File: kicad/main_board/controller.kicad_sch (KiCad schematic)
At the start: 44 parts, among them J6 FRONT_PANEL, J7 I2C, J8 SWD, U7 MCP4728, U8 RP2040, U9 W25Q128JVP, Y1 12MHz

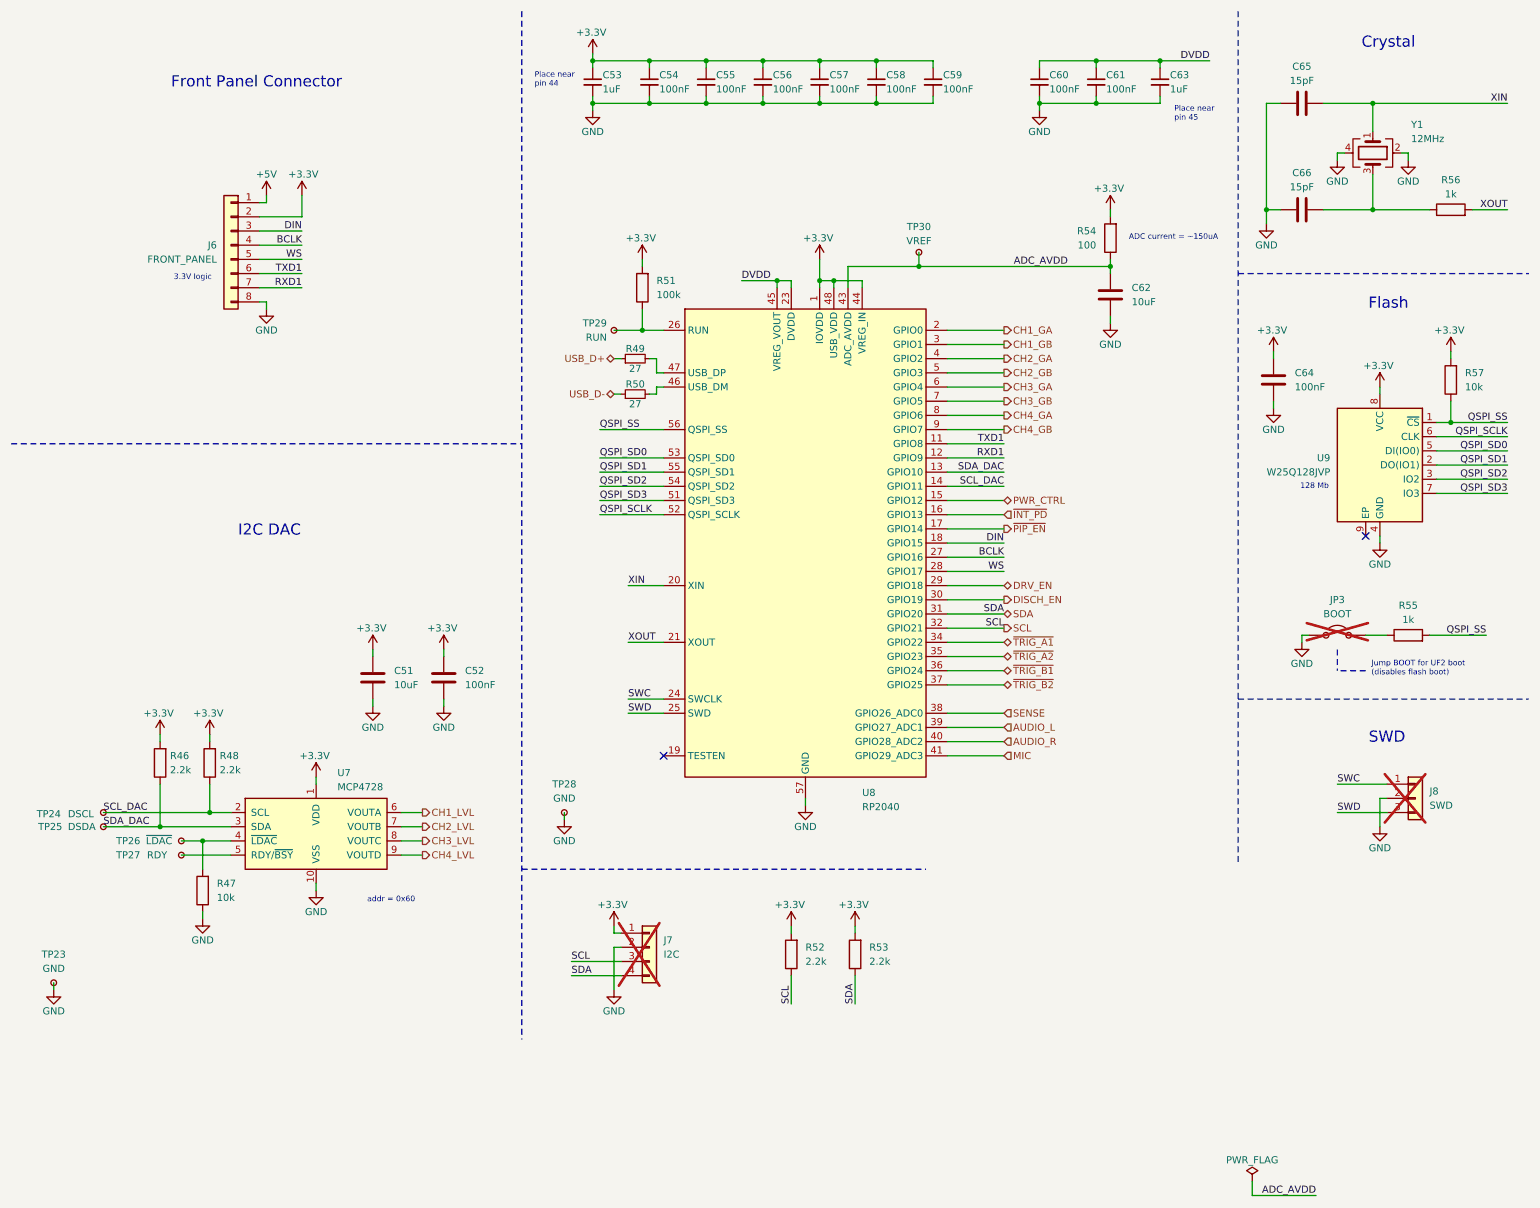
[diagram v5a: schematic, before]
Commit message: remove BAT_INT
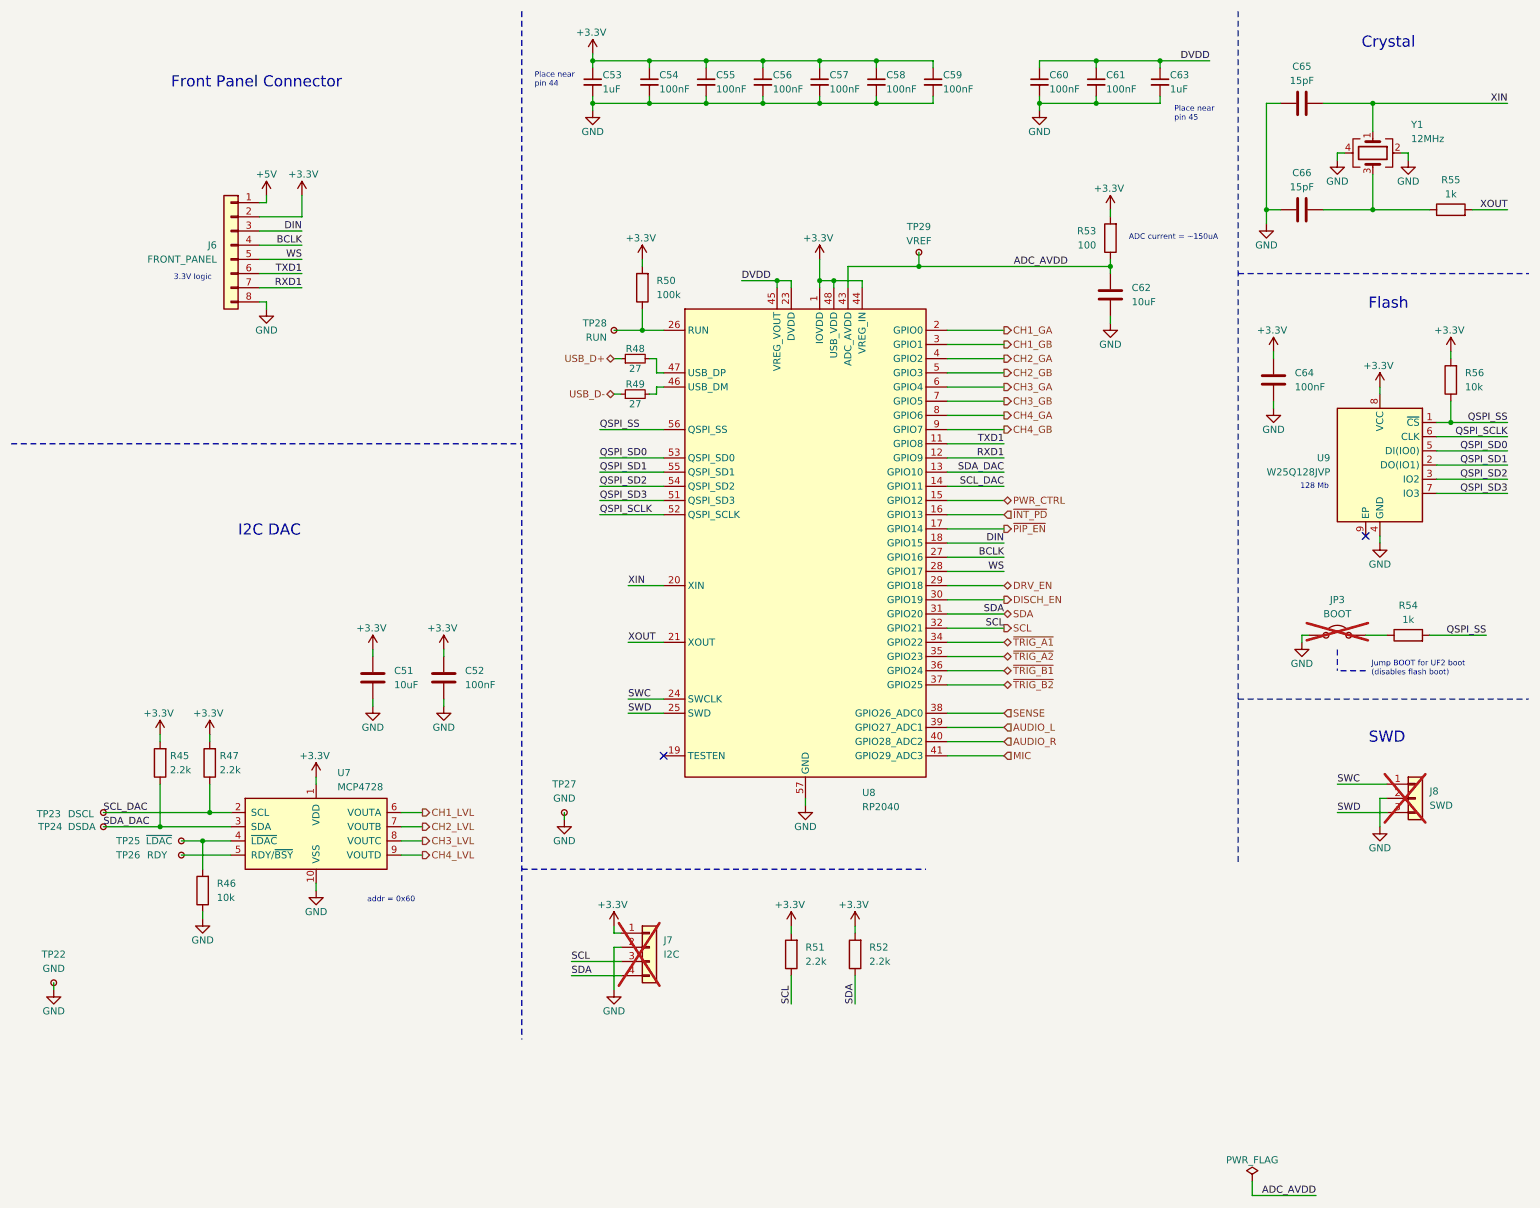
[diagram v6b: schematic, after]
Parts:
- renumbered R46 to R45, R47 to R46, R48 to R47, R49 to R48, R50 to R49, R51 to R50, R52 to R51, R53 to R52, R54 to R53, R55 to R54, R56 to R55, R57 to R56, TP23 to TP22, TP24 to TP23, TP25 to TP24, TP26 to TP25, TP27 to TP26, TP28 to TP27, TP29 to TP28, TP30 to TP29

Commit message: update BOM prioritizing basic parts
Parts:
- C51, C62: JLC (none) -> C96446; LCSC C96446 -> (none); MOUSER 187-CL10A106MA8NRNC -> (none); MPN CL10A106MA8NRNC -> (none)
- C52, C64: JLC (none) -> C14663; LCSC C1591 -> (none); MOUSER 187-CL10B104KB8NNNC -> (none); MPN CL10B104KB8NNNC -> (none)
- C53, C63: JLC (none) -> C15849; LCSC C5199872 -> (none); MOUSER 187-CL10B105KB8NQNC -> (none); MPN CL10B105KB8NQNC -> (none)
- C54, C55, C56, C57, C58, C59, C60, C61: JLC (none) -> C307331; LCSC C960916 -> (none); MOUSER 187-CL05B104KB5NNNC -> (none); MPN CL05B104KB5NNNC -> (none)
- C65, C66: JLC (none) -> C1644; LCSC C1644 -> (none); MOUSER 187-CL10C150JB8NNNC -> (none); MPN CL10C150JB8NNNC -> (none)
- J6: footprint Connector_JST:JST_PH_B8B-PH-K_1x08_P2.00mm_Vertical -> Connector_JST:JST_XH_B8B-XH-A_1x08_P2.50mm_Vertical; LCSC (none) -> C7429638
- J7: LCSC (none) -> C2691448
- J8: LCSC (none) -> C2937625
- JP3: LCSC (none) -> C492401
- R45, R47, R51, R52: JLC (none) -> C4190; LCSC C4190 -> (none); MOUSER 603-RC0603FR-072K2L -> (none); MPN RC0603FR-072K2L -> (none)
- R46, R56: JLC (none) -> C25804; LCSC C25804 -> (none); MOUSER 603-RC0603FR-0710KL -> (none); MPN RC0603FR-0710KL -> (none)
- R48, R49: JLC (none) -> C25190; LCSC C137753 -> (none); MOUSER 603-RC0603FR-0727RL -> (none); MPN RC0603FR-0727RL -> (none)
- R50: JLC (none) -> C25803; LCSC C25803 -> (none); MOUSER 603-RC0603FR-07100KL -> (none); MPN RC0603FR-07100KL -> (none)
- R53: JLC (none) -> C22775; LCSC C22775 -> (none); MOUSER 603-RC0603FR-13100RL -> (none); MPN RC0603FR-07100RL -> (none)
- R54, R55: JLC (none) -> C21190; LCSC C21190 -> (none); MOUSER 603-RC0603FR-071KL -> (none); MPN RC0603FR-071KL -> (none)
- U7: JLC (none) -> C108207; LCSC C108207 -> (none); MOUSER 579-MCP4728-E/UN -> (none); MPN MCP4728-E/UN -> (none)
- U8: JLC (none) -> C2040; LCSC C2040 -> (none); MOUSER 358-SC091413 -> (none); MPN SC0914 -> (none)
- U9: JLC (none) -> C190862; LCSC C190862 -> (none); MOUSER 454-W25Q128JVPIQ -> (none); MPN W25Q128JVPIQ -> (none)
- Y1: JLC (none) -> C20625731; LCSC C20625731 -> (none); MOUSER 815-ABM8-272-T3 -> (none); MPN ABM8-272-T3 -> (none)

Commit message: add generation script
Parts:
- C51, C62: JLC C96446 -> (none); LCSC (none) -> C96446; Service (none) -> PCBA
- C52, C64: JLC C14663 -> (none); LCSC (none) -> C14663; Service (none) -> PCBA
- C53, C63: JLC C15849 -> (none); LCSC (none) -> C15849; Service (none) -> PCBA
- C54, C55, C56, C57, C58, C59, C60, C61: JLC C307331 -> (none); LCSC (none) -> C307331; Service (none) -> PCBA
- C65, C66: JLC C1644 -> (none); LCSC (none) -> C1644; Service (none) -> PCBA
- J6, J7, J8, JP3: Service (none) -> HandAssembly
- R45, R47, R51, R52: JLC C4190 -> (none); LCSC (none) -> C4190; Service (none) -> PCBA
- R46, R56: JLC C25804 -> (none); LCSC (none) -> C25804; Service (none) -> PCBA
- R48, R49: JLC C25190 -> (none); LCSC (none) -> C25190; Service (none) -> PCBA
- R50: JLC C25803 -> (none); LCSC (none) -> C25803; Service (none) -> PCBA
- R53: JLC C22775 -> (none); LCSC (none) -> C22775; Service (none) -> PCBA
- R54, R55: JLC C21190 -> (none); LCSC (none) -> C21190; Service (none) -> PCBA
- TP22, TP23, TP24, TP25, TP26, TP27, TP28, TP29: Service (none) -> PCBA;HandAssembly
- U7: JLC C108207 -> (none); LCSC (none) -> C108207; Service (none) -> PCBA
- U8: JLC C2040 -> (none); LCSC (none) -> C2040; Service (none) -> PCBA
- U9: JLC C190862 -> (none); LCSC (none) -> C190862; Service (none) -> PCBA
- Y1: JLC C20625731 -> (none); LCSC (none) -> C20625731; Service (none) -> PCBA
